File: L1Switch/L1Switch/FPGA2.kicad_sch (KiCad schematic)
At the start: 1 part, among them U1 XC7A15T-FTG256

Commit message: Most signals routed.
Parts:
- added C376, C377: 100nF, Capacitor_SMD:C_0402_1005Metric, symbol Device:C
- added J10: Conn_02x07_Odd_Even, Connector_PinHeader_2.00mm:PinHeader_2x07_P2.00mm_Vertical, symbol Connector_Generic:Conn_02x07_Odd_Even
- added R256, R257, R258: 2K0, Resistor_SMD:R_0402_1005Metric, symbol Device:R_US
- added U10: W25Q128JVS, Package_SO:SOIC-8_5.23x5.23mm_P1.27mm, symbol Memory_Flash:W25Q128JVS
- added U11: TXB0108PW, Package_SO:TSSOP-20_4.4x6.5mm_P0.65mm, symbol Logic_LevelTranslator:TXS0108EPW
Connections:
- net GND: now also U1.M10 (M1_0), U1.M11 (M2_0), C376.1, C377.2, J10.1 (Pin_1), J10.11 (Pin_11), J10.13 (Pin_13), J10.3 (Pin_3), J10.5 (Pin_5), J10.7 (Pin_7), J10.9 (Pin_9), U10.4 (GND), U11.11 (GND), U11.12 (B8), U11.13 (B7), U11.14 (B6), U11.7 (A6), U11.8 (A7), U11.9 (A8)
- net SPI_CLK: now reaches U1.E8 (CCLK_0)
- net SPI_CLK: now also U10.6 (CLK)
- net +3V3: now reaches U1.L6 (VCCO_0)
- net +3V3: now also U1.M9 (M0_0), C377.1, J10.2 (Pin_2), R257.1, R258.1, U10.8 (VCC), U11.19 (VCCB)
- net FPGA_TCK: now reaches U1.L7 (TCK_0)
- net FPGA_TCK: now also J10.6 (Pin_6)
- net FPGA_TMS: now reaches U1.M7 (TMS_0)
- net FPGA_TMS: now also J10.4 (Pin_4)
- net FPGA_TDI: now reaches U1.N7 (TDI_0)
- net FPGA_TDI: now also J10.10 (Pin_10)
- net FPGA_TDO: now reaches U1.N8 (TDO_0)
- net FPGA_TDO: now also J10.8 (Pin_8)
- new net +1V2: C376.2, R256.1, U11.10 (OE), U11.2 (VCCA)
- new net CS_N: R256.2, U11.1 (A1)
- new net DI: U11.6 (A5)
- new net DO: U11.5 (A4)
- new net HOLD_N: U11.3 (A2)
- new net SPI_CS_N: U10.1 (~CS), U11.20 (B1)
- new net SPI_IO0: U10.5 (DI(IO0)), U11.15 (B5)
- new net SPI_IO1: U10.2 (DO(IO1)), U11.16 (B4)
- new net SPI_IO2: R257.2, U10.3 (IO2), U11.17 (B3)
- new net SPI_IO3: R258.2, U10.7 (IO3), U11.18 (B2)
- new net W_N: U11.4 (A3)
- no-connect marks 0 -> 2

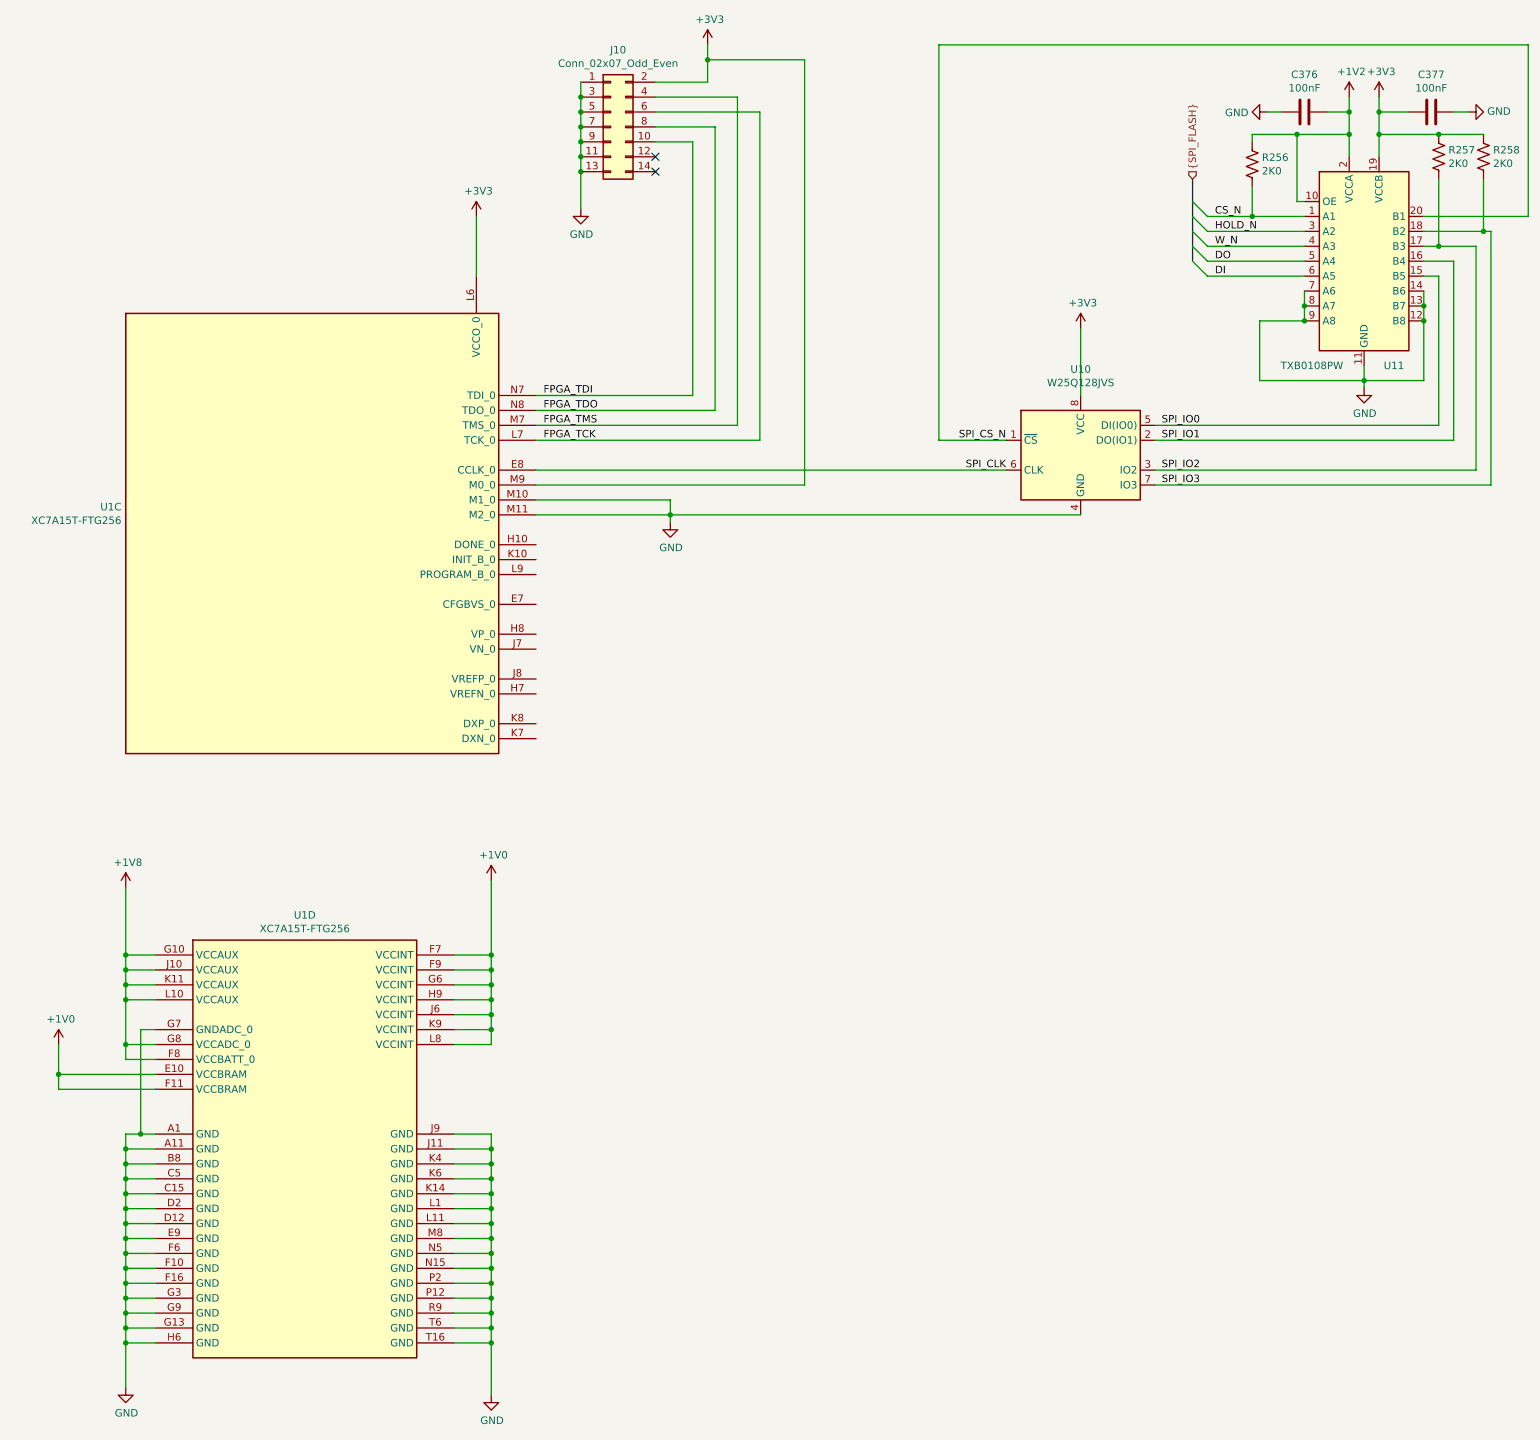
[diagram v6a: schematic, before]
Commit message: Switch to XC7A35T. Update some layout constraints for 4pcb.com capabilities.
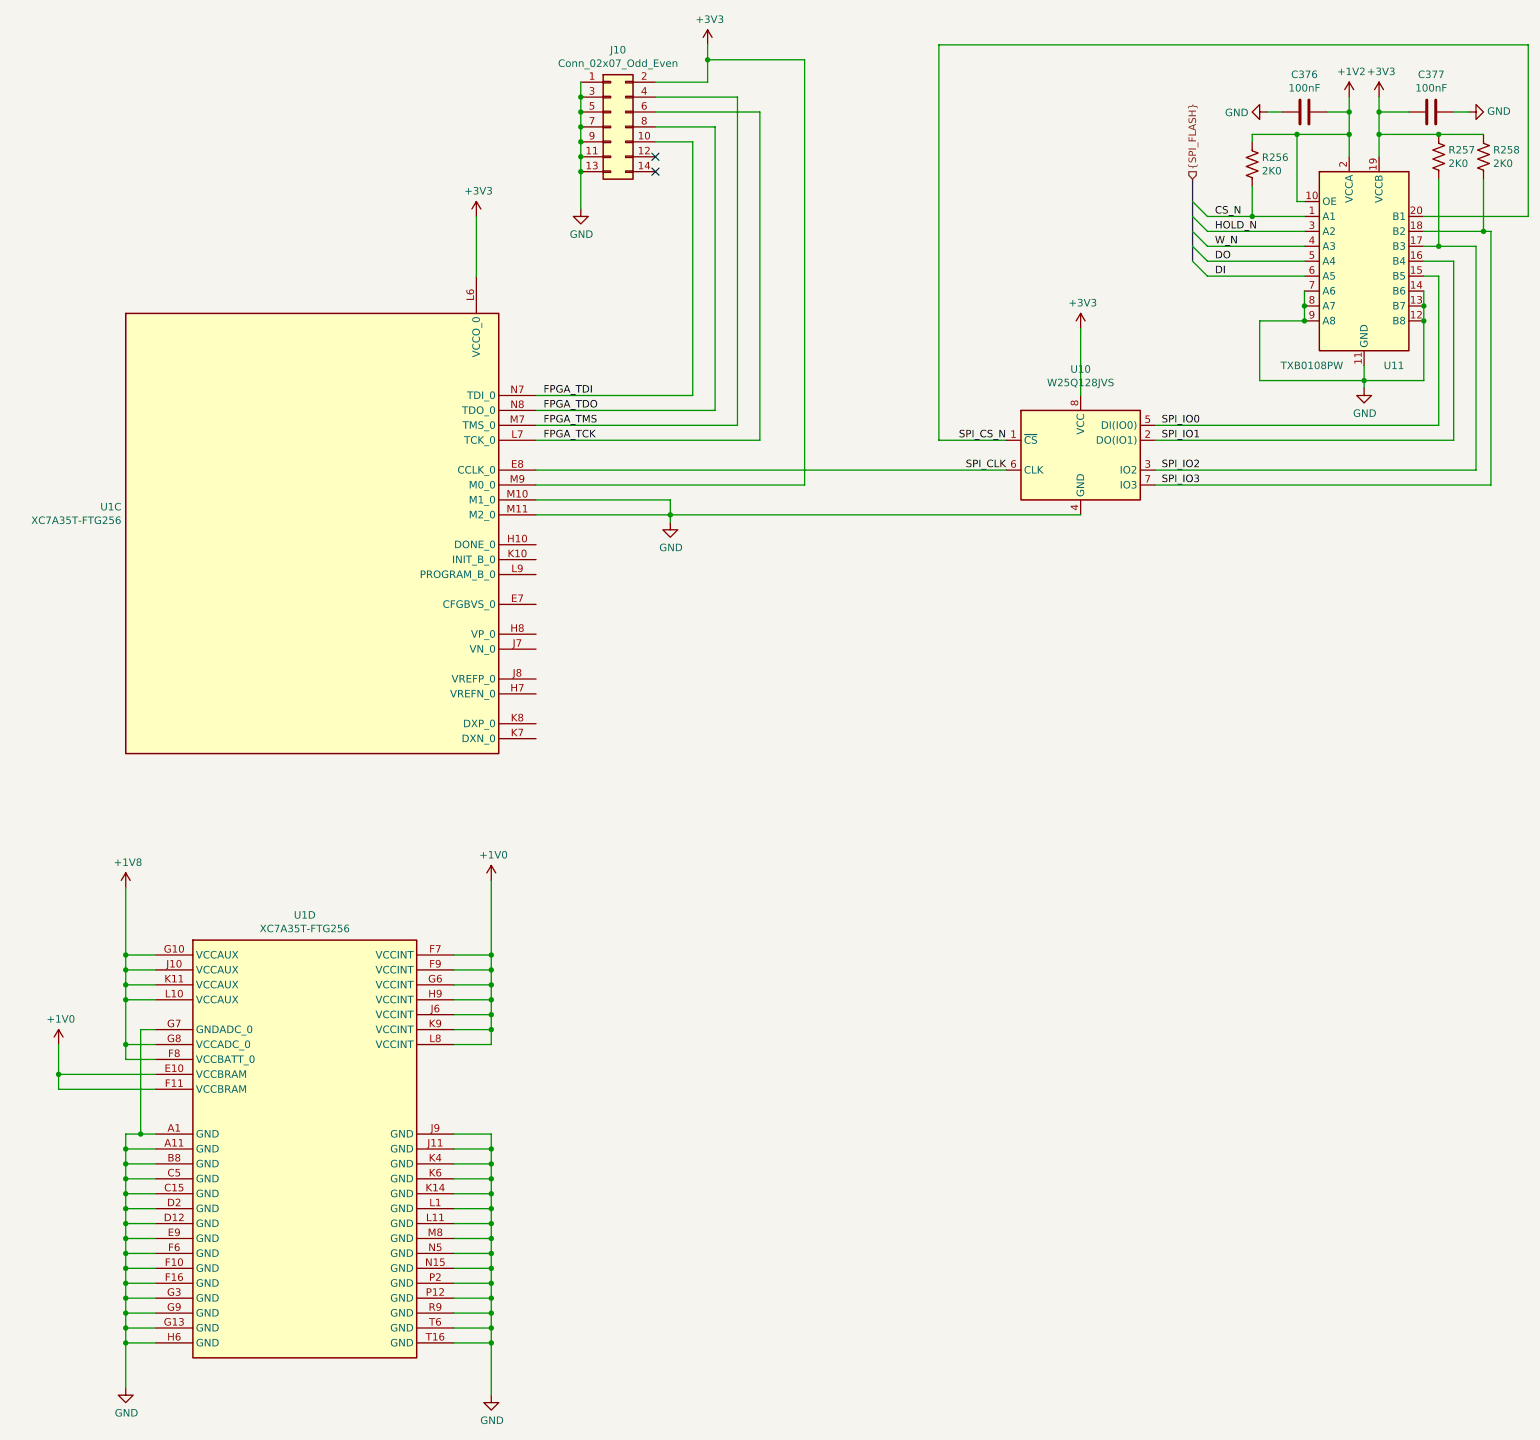
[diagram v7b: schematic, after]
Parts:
- U1: value XC7A15T-FTG256 -> XC7A35T-FTG256; symbol FPGA_Xilinx_Artix7:XC7A15T-FTG256 -> FPGA_Xilinx_Artix7:XC7A35T-FTG256
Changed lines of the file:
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@@
   (junction (at 387.35 54.61))
   (junction (at 394.97 52.07))
+  (no_connect (at 254 41.91))
   (no_connect (at 254 39.37))
-  (no_connect (at 254 41.91))
   (bus_entry (at 347.98 49.53) (size -2.54 -2.54))
   (bus_entry (at 347.98 52.07) (size -2.54 -2.54))
@@
     (stroke (width 0) (type solid) (color 0 0 0 0))
   )
-  (bus (pts (xy 345.44 43.18) (xy 345.44 46.99))
-    (stroke (width 0) (type solid) (color 0 0 0 0))
-  )
-  (bus (pts (xy 345.44 46.99) (xy 345.44 52.07))
-    (stroke (width 0) (type solid) (color 0 0 0 0))
-  )
-  (bus (pts (xy 345.44 52.07) (xy 345.44 57.15))
+  (bus (pts (xy 345.44 43.18) (xy 345.44 49.53))
+    (stroke (width 0) (type solid) (color 0 0 0 0))
+  )
+  (bus (pts (xy 345.44 49.53) (xy 345.44 54.61))
+    (stroke (width 0) (type solid) (color 0 0 0 0))
+  )
+  (bus (pts (xy 345.44 54.61) (xy 345.44 57.15))
     (stroke (width 0) (type solid) (color 0 0 0 0))
   )
@@
     )
   )
-  (symbol (lib_id "FPGA_Xilinx_Artix7:XC7A15T-FTG256") (at 194.31 208.28 0) (unit 4)
+  (symbol (lib_id "FPGA_Xilinx_Artix7:XC7A35T-FTG256") (at 194.31 208.28 0) (unit 4)
     (in_bom yes) (on_board yes)
     (property "Reference" "U1" (id 0) (at 194.31 168.4782 0))
-    (property "Value" "XC7A15T-FTG256" (id 1) (at 194.31 170.7896 0))
+    (property "Value" "XC7A35T-FTG256" (id 1) (at 194.31 170.7896 0))
     (property "Footprint" "Package_BGA:Xilinx_FTG256" (id 2) (at 194.31 208.28 0)
       (effects (font (size 1.27 1.27)) hide)
@@
     (property "Datasheet" "" (id 3) (at 194.31 208.28 0))
   )
-  (symbol (lib_id "FPGA_Xilinx_Artix7:XC7A15T-FTG256") (at 195.58 100.33 0) (unit 3)
+  (symbol (lib_id "FPGA_Xilinx_Artix7:XC7A35T-FTG256") (at 195.58 100.33 0) (unit 3)
     (in_bom yes) (on_board yes)
     (property "Reference" "U1" (id 0) (at 163.0934 98.9838 0)
       (effects (font (size 1.27 1.27)) (justify right))
     )
-    (property "Value" "XC7A15T-FTG256" (id 1) (at 163.0934 101.2952 0)
+    (property "Value" "XC7A35T-FTG256" (id 1) (at 163.0934 101.2952 0)
       (effects (font (size 1.27 1.27)) (justify right))
     )
